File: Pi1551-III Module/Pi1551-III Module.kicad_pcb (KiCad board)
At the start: 2 copper layers, 100 x 100 mm, 25 parts, among them J1 DC IN, J2 C64_IEC, J3 C64_IEC, J8 Module_Panel, M1 Mounting, M2 Mounting, M3 Mounting, M4 Mounting, U1 7406

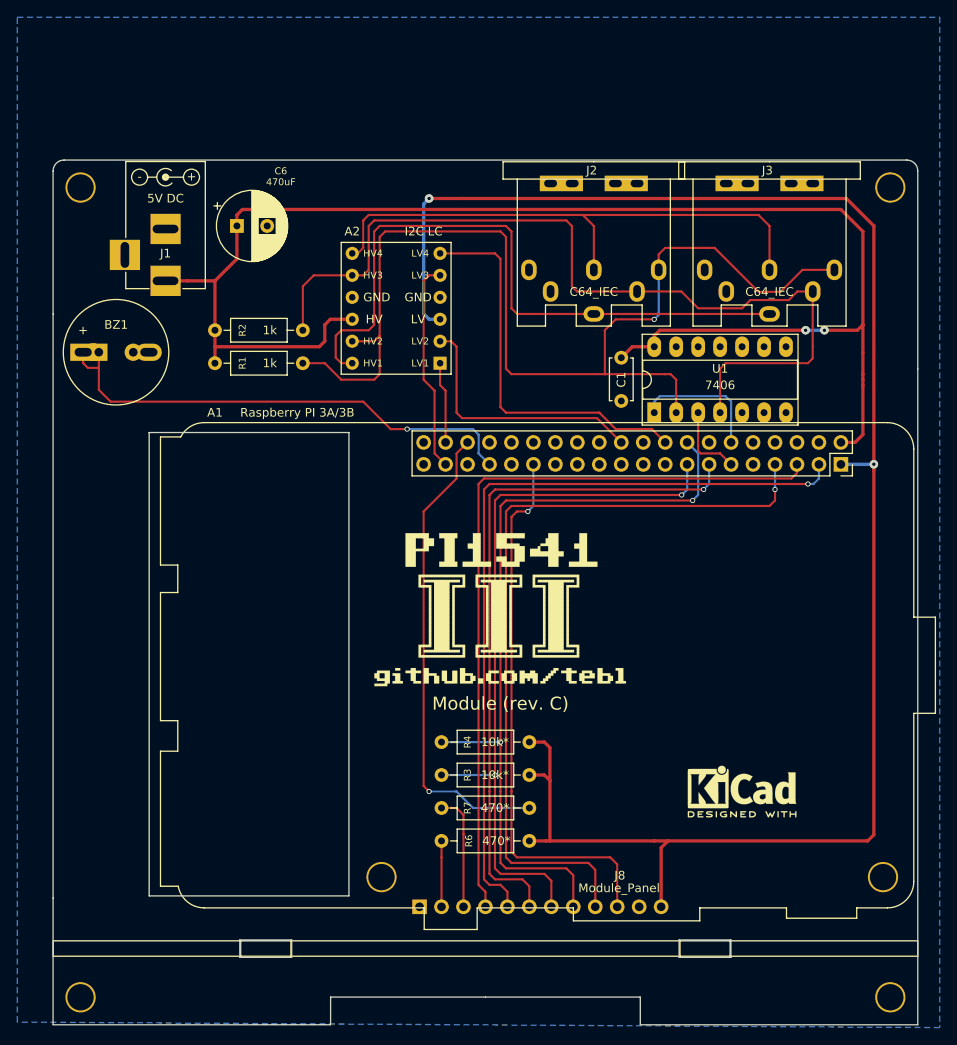
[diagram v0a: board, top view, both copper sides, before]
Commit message: upgrade to KiCad 9.0.7
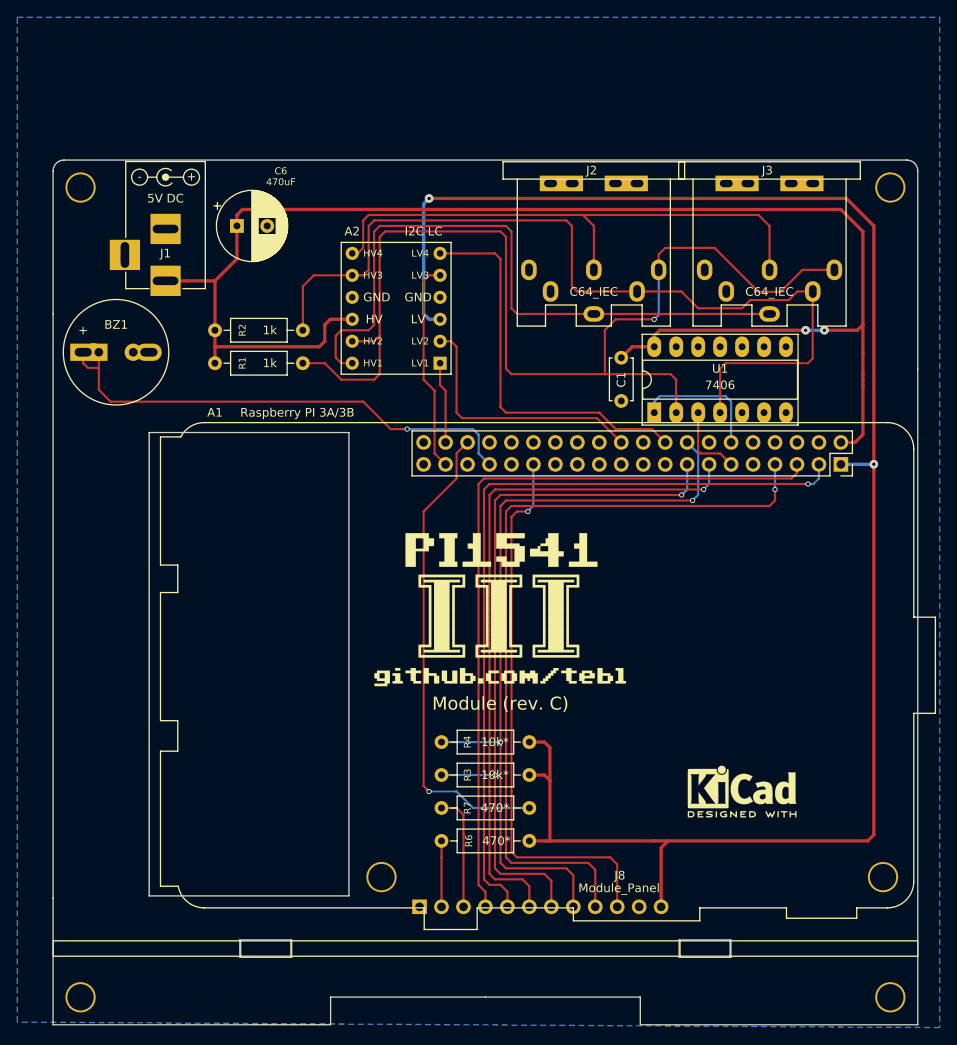
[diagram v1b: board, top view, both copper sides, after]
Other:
- net class Default removed
- net class Power removed
